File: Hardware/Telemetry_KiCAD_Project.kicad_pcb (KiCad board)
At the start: 4 copper layers, 80 x 93.3 mm, 81 parts, among them J1 TX SPI Debug, J2 RX SPI Debug, J3 Amphenol 132134 SMA Connector, J4 10118192-0001LF, J5 DB37_Male_MountingHoles, SW1 MCU Reset, U1 Si4463, U2 ADL5521, U3 RSD-897.500-942.500-1612-TR, U4 LM317T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

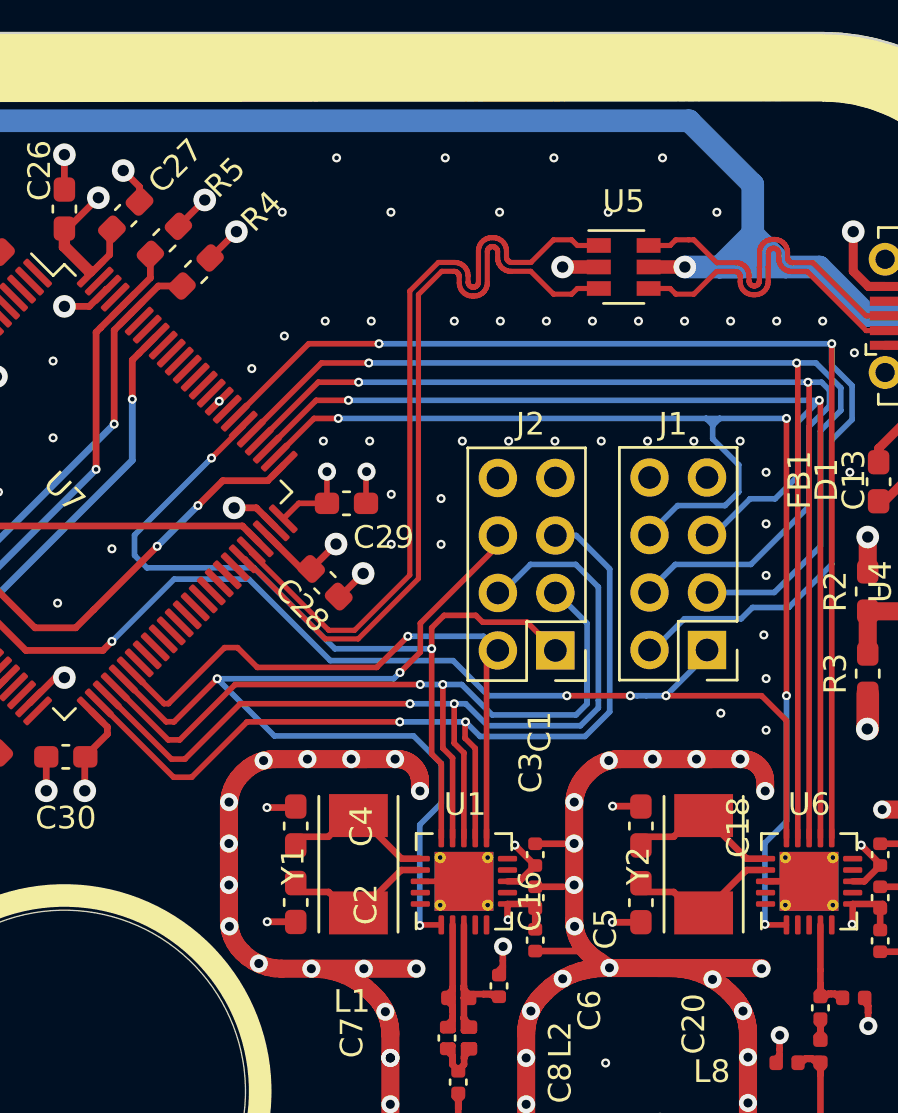
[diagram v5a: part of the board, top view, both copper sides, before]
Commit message: Added header pins for PH3 bootloader toggling
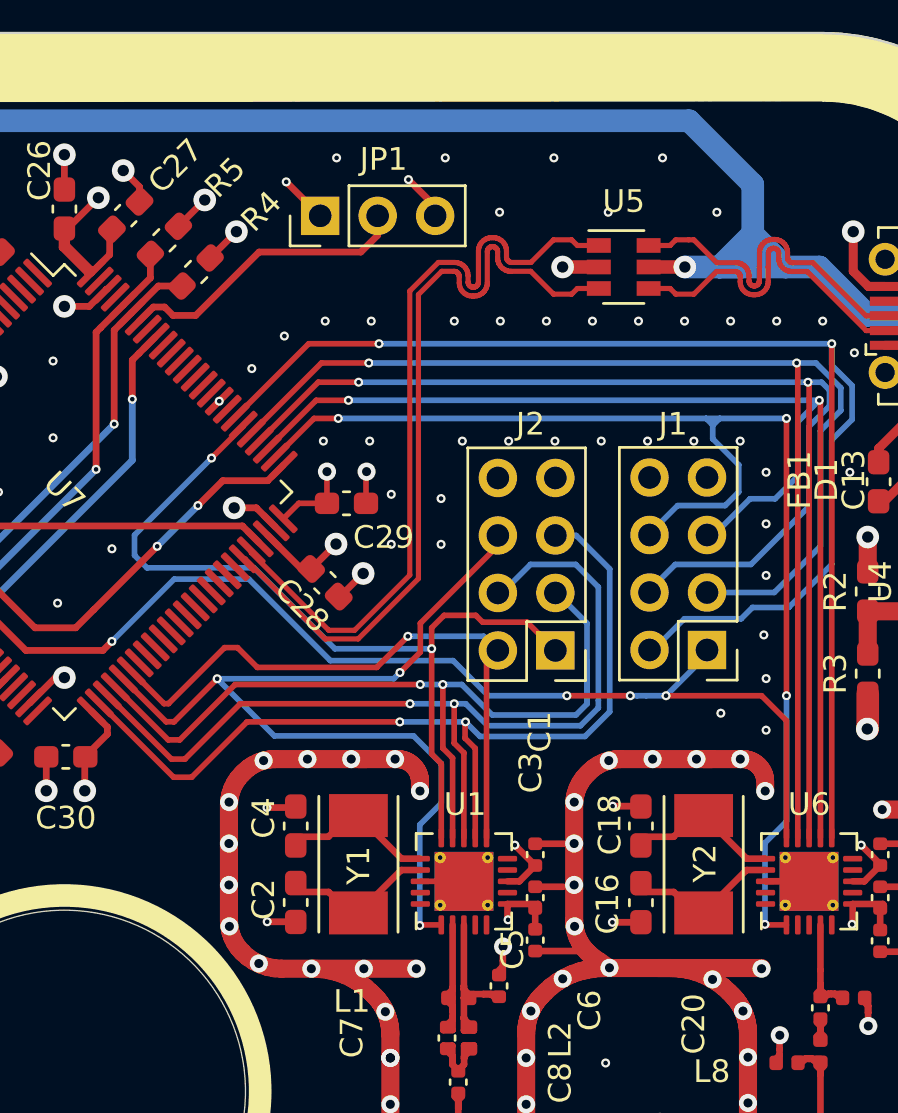
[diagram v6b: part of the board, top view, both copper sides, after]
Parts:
- added JP1: Debug Jumper, Connector_PinHeader_2.54mm:PinHeader_1x03_P2.54mm_Vertical, F.Cu at (127.8, 59.8)
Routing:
- net Net-(JP1-Pad2): track 0.00 -> 13.3 mm
- net GND: track 322.9 -> 325.0 mm, vias 375 -> 374
- net +3V3: track 57.6 -> 59.7 mm, vias 16 -> 17

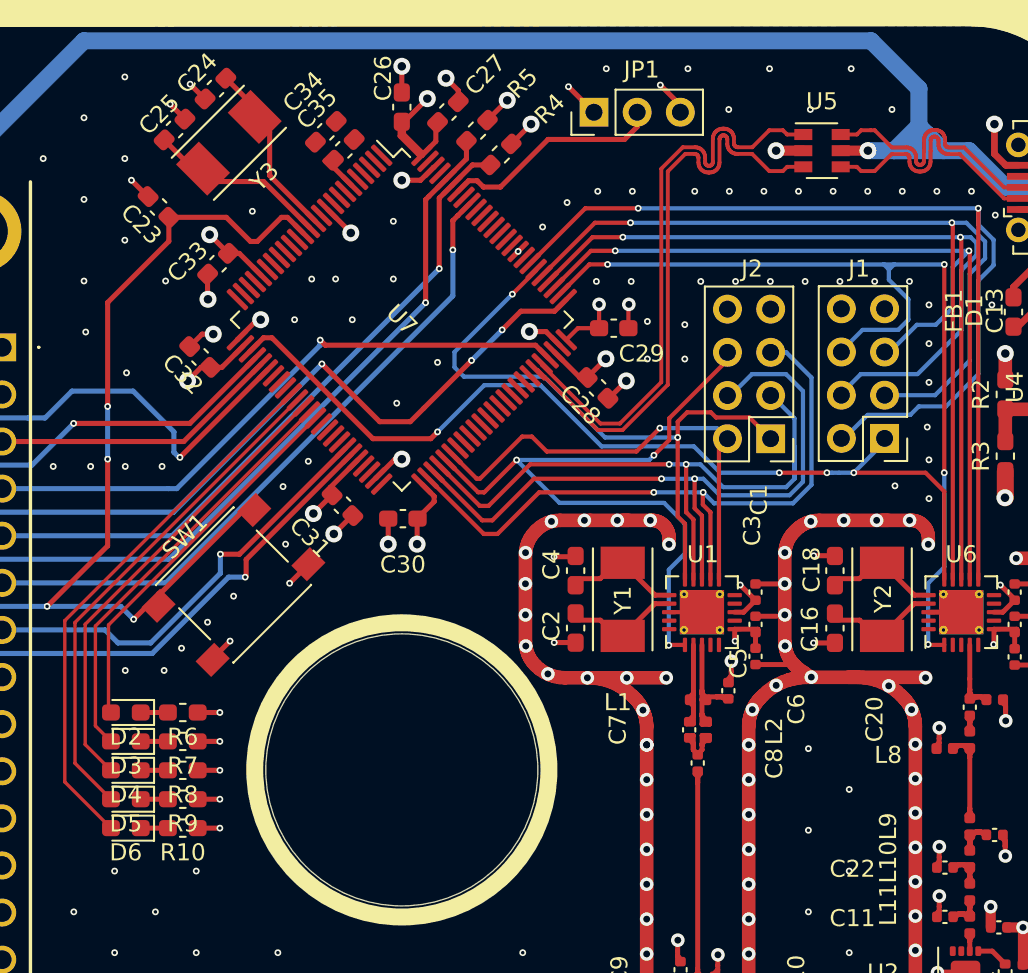
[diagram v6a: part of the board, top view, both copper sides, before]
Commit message: Connected unconnected MCU filter caps
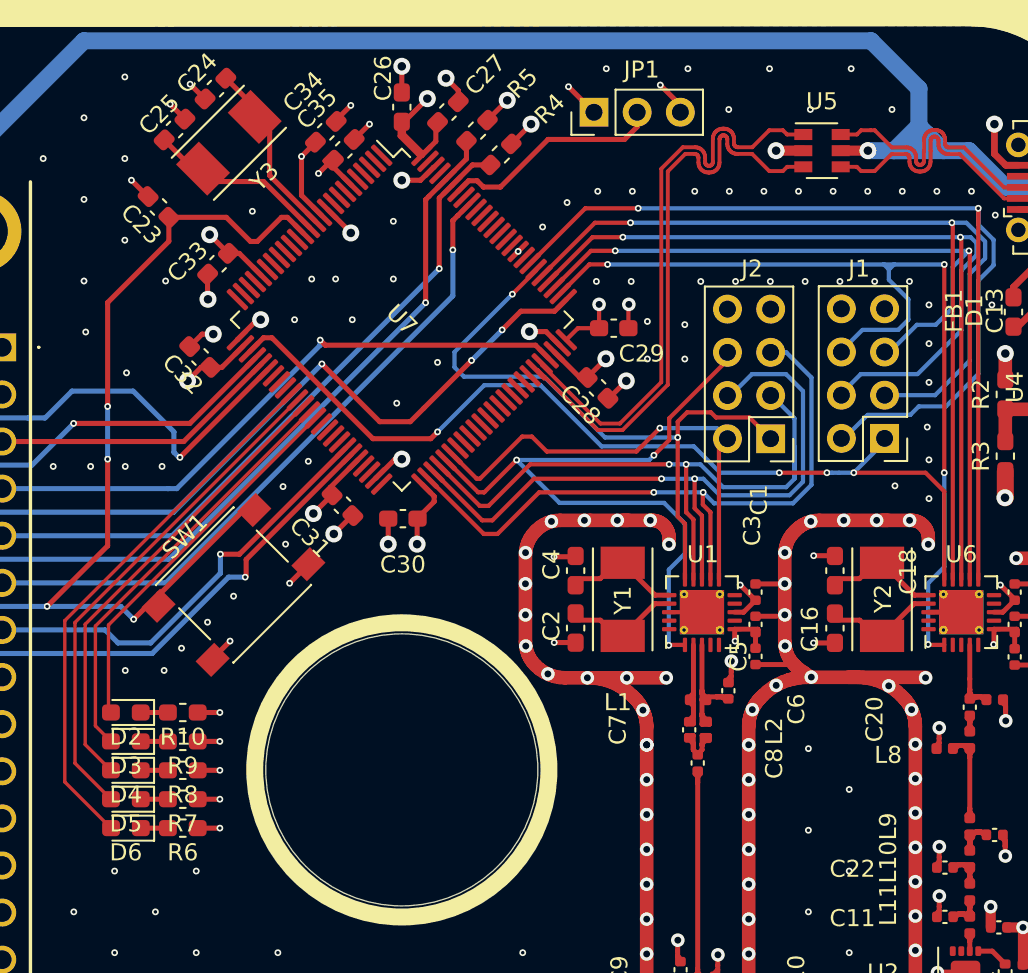
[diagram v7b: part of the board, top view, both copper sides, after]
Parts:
- moved R10 6.80 mm to (103.6, 95.1)
- moved R6 6.80 mm to (103.6, 101.9)
- moved R7 3.40 mm to (103.6, 100.2)
- moved R9 3.40 mm to (103.6, 96.8)
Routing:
- net +3V3: track 59.7 -> 66.0 mm, vias 17 -> 19
- net GND: track 325.0 -> 327.5 mm, vias 374 -> 376
